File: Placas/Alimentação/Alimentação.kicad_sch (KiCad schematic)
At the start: 4 parts, among them J1 Conn_02x02_ZigZag, J2 Conn_02x03_ZigZag, J3 Conn_02x02_ZigZag, J4 Conn_02x01

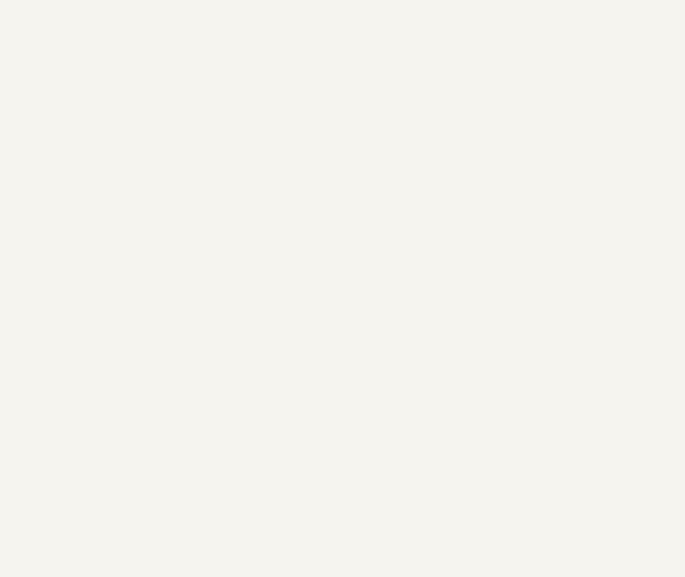
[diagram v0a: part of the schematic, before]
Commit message: Modificações nas duas placas, adição de furos para montagem, melhora na posição dos micros e conectores para comunicação SPI
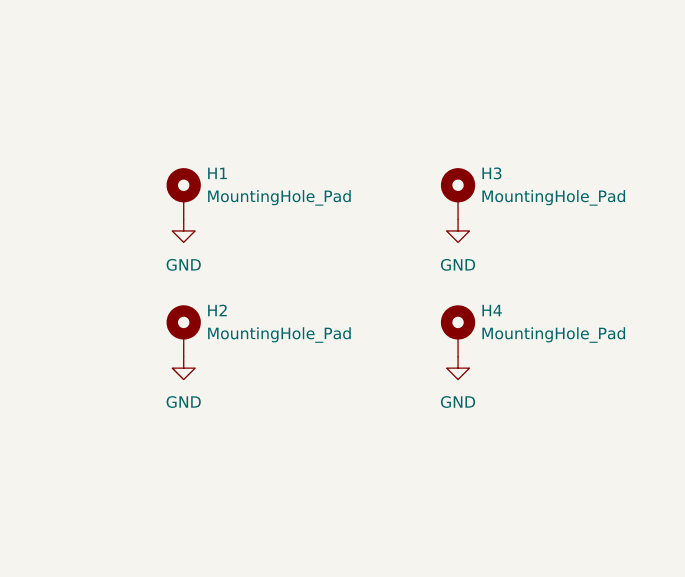
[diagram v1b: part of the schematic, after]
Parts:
- added H1, H2, H3, H4: MountingHole_Pad, MountingHole:MountingHole_3.2mm_M3_Pad_Via, symbol Mechanical:MountingHole_Pad
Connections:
- net GND: now also H1.1, H2.1, H3.1, H4.1
